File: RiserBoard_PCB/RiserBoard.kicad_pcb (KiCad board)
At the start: 2 copper layers, 31.1 x 14 mm, 10 parts, among them J1 BUS1, J2 AudioJack3, J3 BUS2

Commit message: Made Naming of Pins consistent
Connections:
- net /B_L renamed /B_T
- net /T_L renamed /T_T

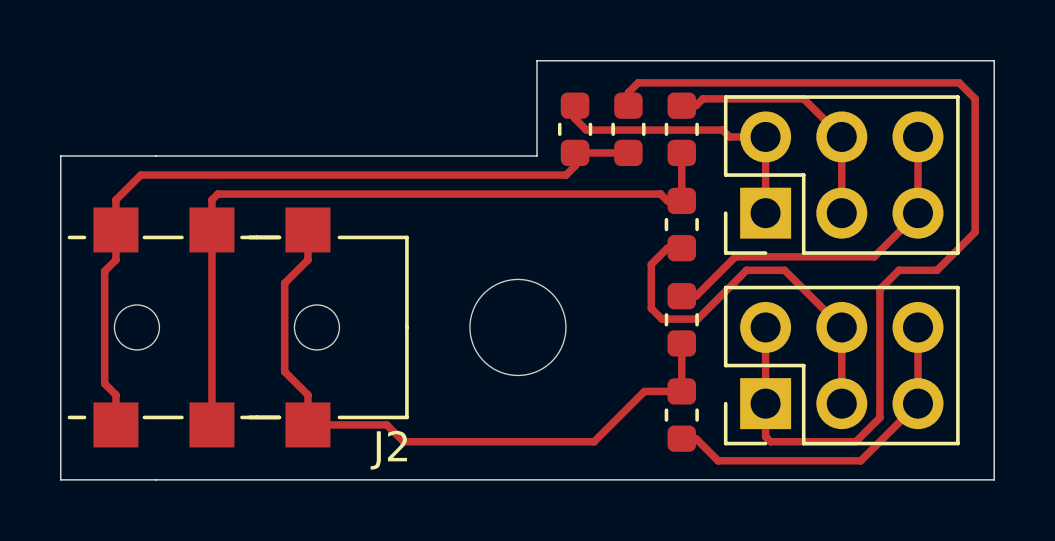
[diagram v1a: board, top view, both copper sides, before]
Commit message: Rearranged Support Screw to fit pinheader under boards
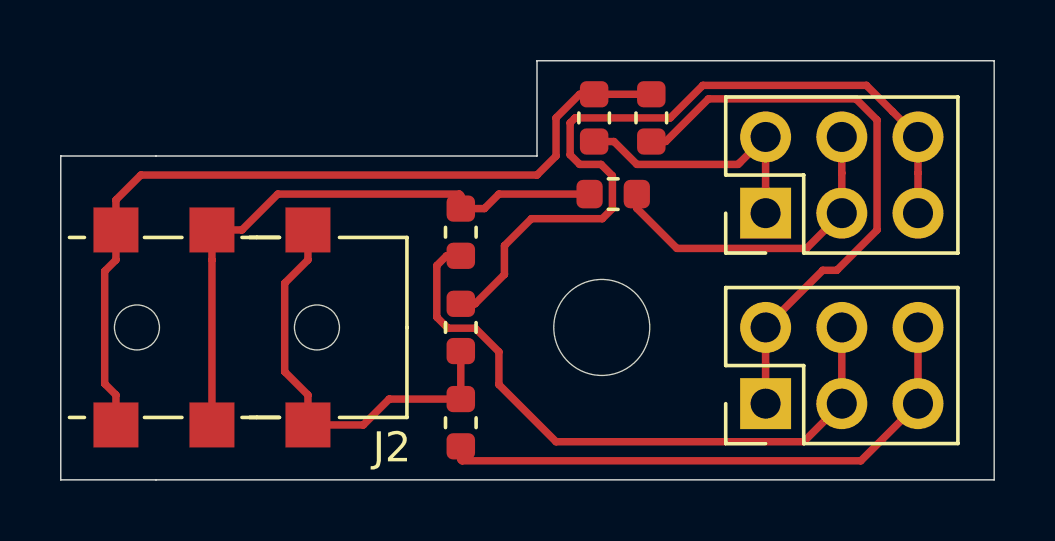
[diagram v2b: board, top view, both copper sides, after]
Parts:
- moved JP3 7.37 mm to (139.7, 95.2)
- moved JP4 7.37 mm to (139.7, 92.1)
- moved JP5 7.37 mm to (139.7, 88.9)
- moved JP6 3.14 mm to (144.8, 87.6), turned to 0 degrees
- moved H1 2.79 mm to (144.4, 92.1)
- moved JP1 0.85 mm to (146.1, 85.1), turned to 90 degrees
- moved JP2 0.74 mm to (144.1, 85.1), turned to 270 degrees
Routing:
- net /B_T: track 11.6 -> 26.2 mm
- net /T_S: track 32.9 -> 19.7 mm
- net /T_R: track 13.2 -> 21.6 mm
- net Net-(J2-PadT): track 22.1 -> 14.2 mm
- net /T_T: track 11.5 -> 19.0 mm
- net Net-(J2-PadR): track 24.9 -> 20.2 mm
- net /B_R: track 8.49 -> 10.9 mm
- net Net-(J2-PadS): track 25.8 -> 27.9 mm
- net /B_S: track 9.58 -> 8.95 mm
